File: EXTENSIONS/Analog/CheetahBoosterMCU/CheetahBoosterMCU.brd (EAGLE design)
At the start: 50 x 79 mm, 11 parts

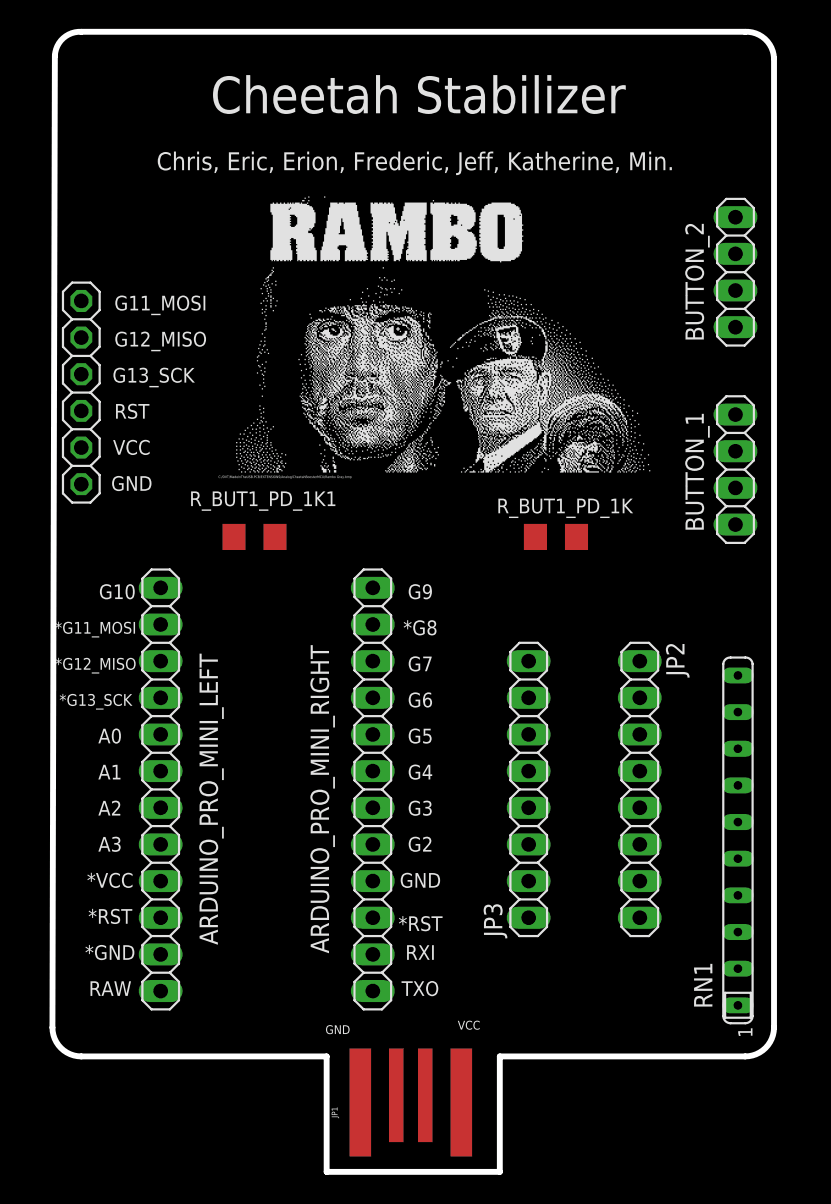
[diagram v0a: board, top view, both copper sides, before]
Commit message: Create CheetahBooster MCU
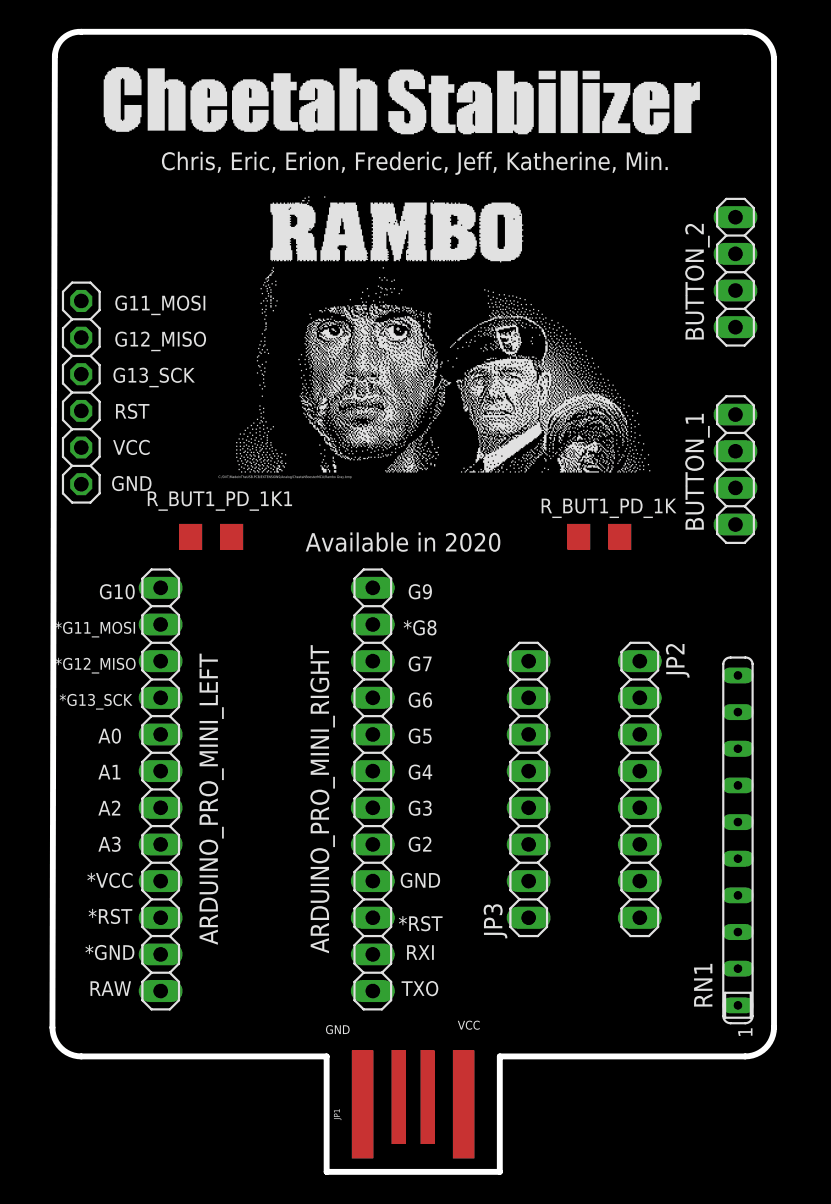
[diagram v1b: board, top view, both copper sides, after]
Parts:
- moved R_BUT1_PD_1K 3.00 mm to (37.9, 45.0)
- moved R_BUT1_PD_1K1 3.00 mm to (11.0, 45.0)
- moved JP1 0.20 mm to (25.0, 5.88)
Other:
- board text added: "Available in 2020"
- board text removed: "Cheetah Stabilizer"
